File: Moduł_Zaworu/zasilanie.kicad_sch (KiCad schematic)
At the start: 25 parts, among them U1 LM2596S-ADJ, U10 LD1117S33TR_SOT223, U3 TLV172IDCK, U4 TL431D, U9 L7805

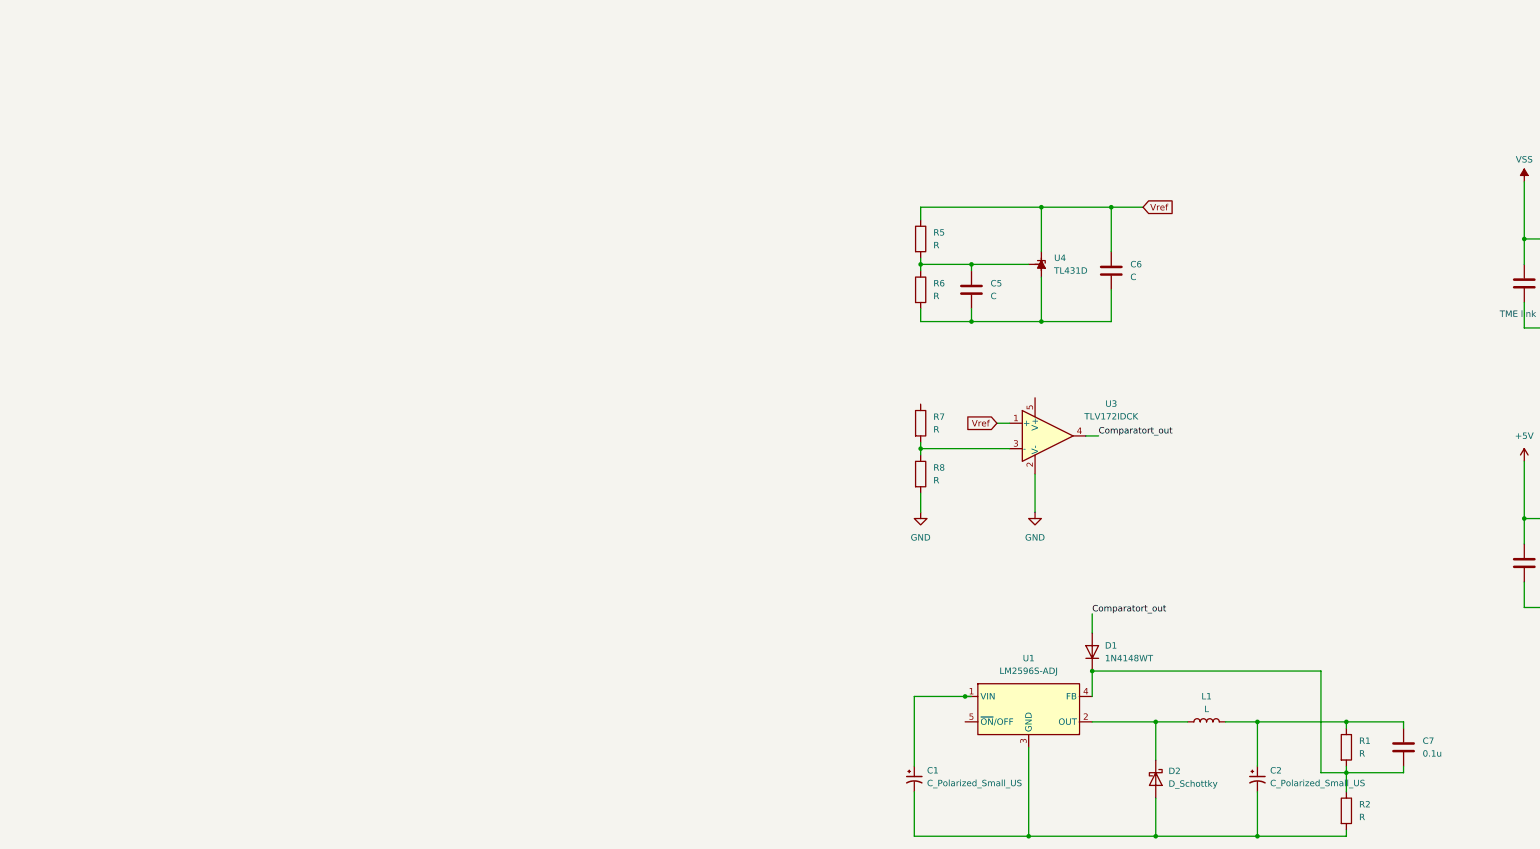
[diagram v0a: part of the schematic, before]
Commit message: Poprawki schematu modułu zaworu, usunięcie przekaźnika, przygotowanie schematu zasilania
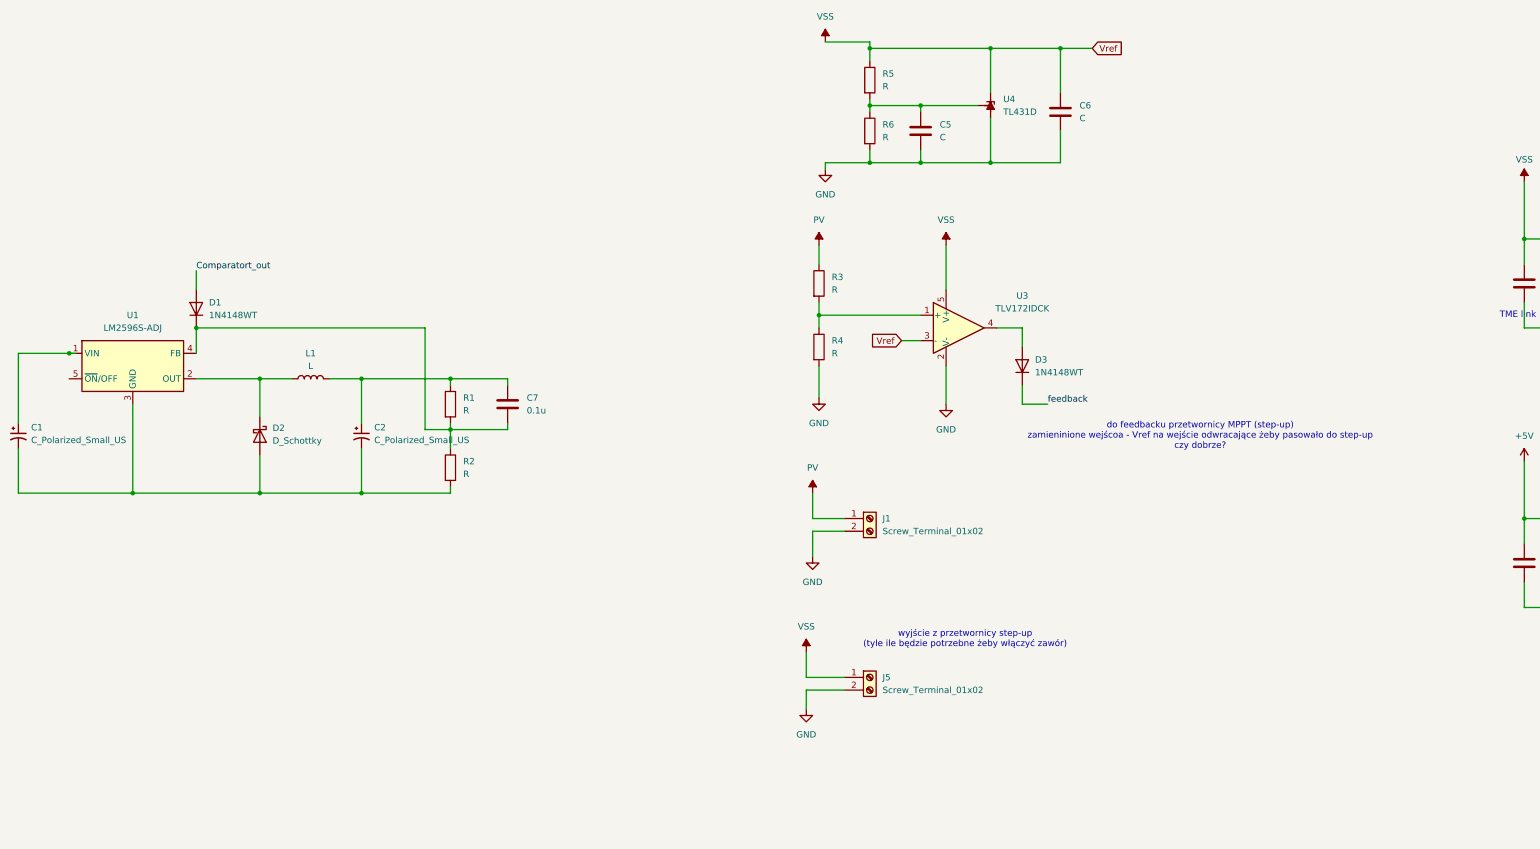
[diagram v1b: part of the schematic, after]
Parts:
- removed R7, R8: R, symbol Device:R
- added D3: 1N4148WT, Diode_SMD:D_SOD-523, symbol Diode:1N4148WT
- added J1, J5: Screw_Terminal_01x02, TerminalBlock:TerminalBlock_MaiXu_MX126-5.0-02P_1x02_P5.00mm, symbol Connector:Screw_Terminal_01x02
- added R3, R4: R, symbol Device:R
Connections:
- net Comparatort_out: no longer U3.4
- net GND: now also C5.2, C6.2, R6.2, U4.2 (A), U4.3 (A), U4.6 (A), U4.7 (A), J1.2 (Pin_2), J5.2 (Pin_2), R4.2
- net VSS: now also C6.1, R5.1, U3.3 (-), U3.5 (V+), U4.1 (K), J5.1 (Pin_1)
- removed net Vref: C6.1, R5.1, U3.1 (+), U4.1 (K)
- new net: R3.2, R4.1, U3.1 (+)
- new net: D3.2 (A), U3.4
- new net PV: J1.1 (Pin_1), R3.1
- new net feedback: D3.1 (K)
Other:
- note added: "do feedbacku przetwornicy MPPT (step-up) zamieninione wejścoa - Vref na wejście odwracające żeby pasowało do step-up czy dobrze?"
- note added: "wyjście z przetwornicy step-up (tyle ile będzie potrzebne żeby włączyć zawór)"
- moved on the sheet: C1, C2, C5, C6, C7, D1, D2, L1, R1, R2, R5, R6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

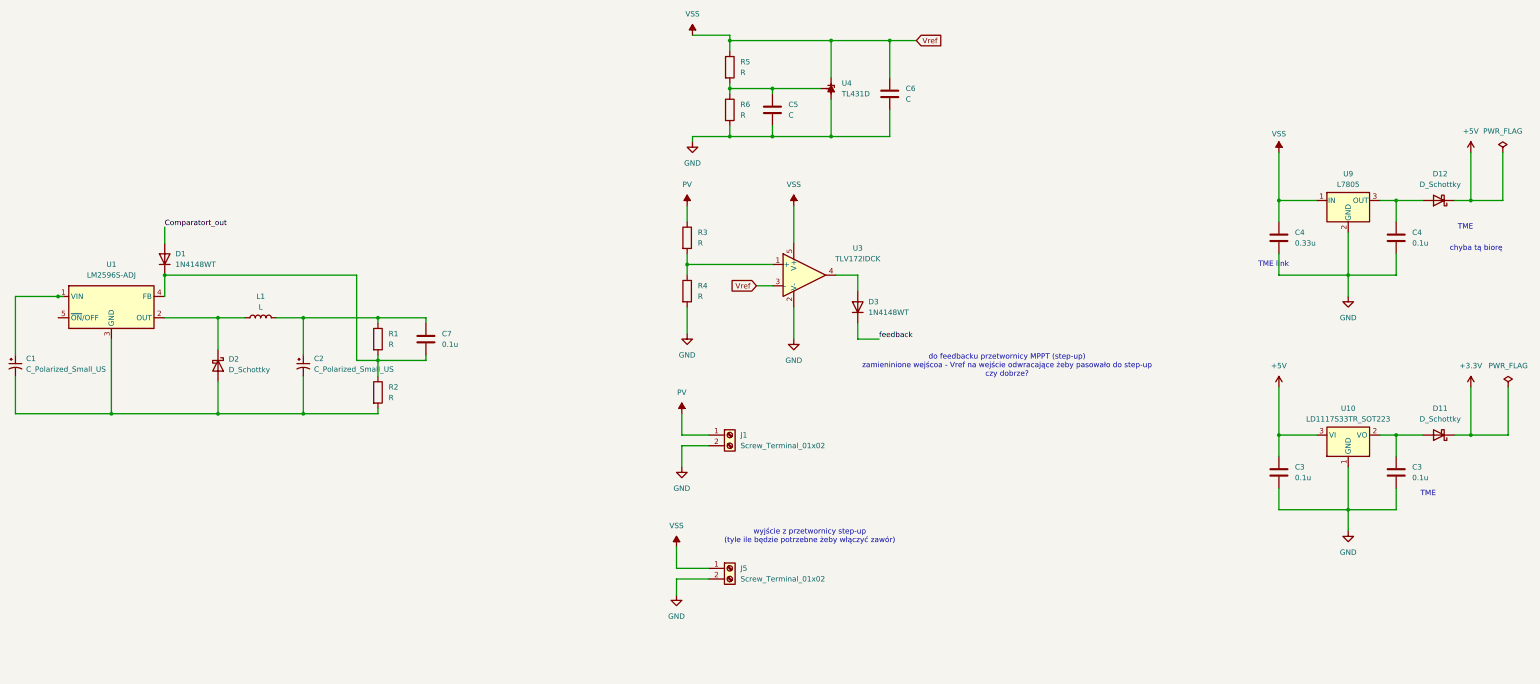
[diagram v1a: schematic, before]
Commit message: Poprawki schematu modułu zaworu, usunięcie przekaźnika, przygotowanie schematu zasilania
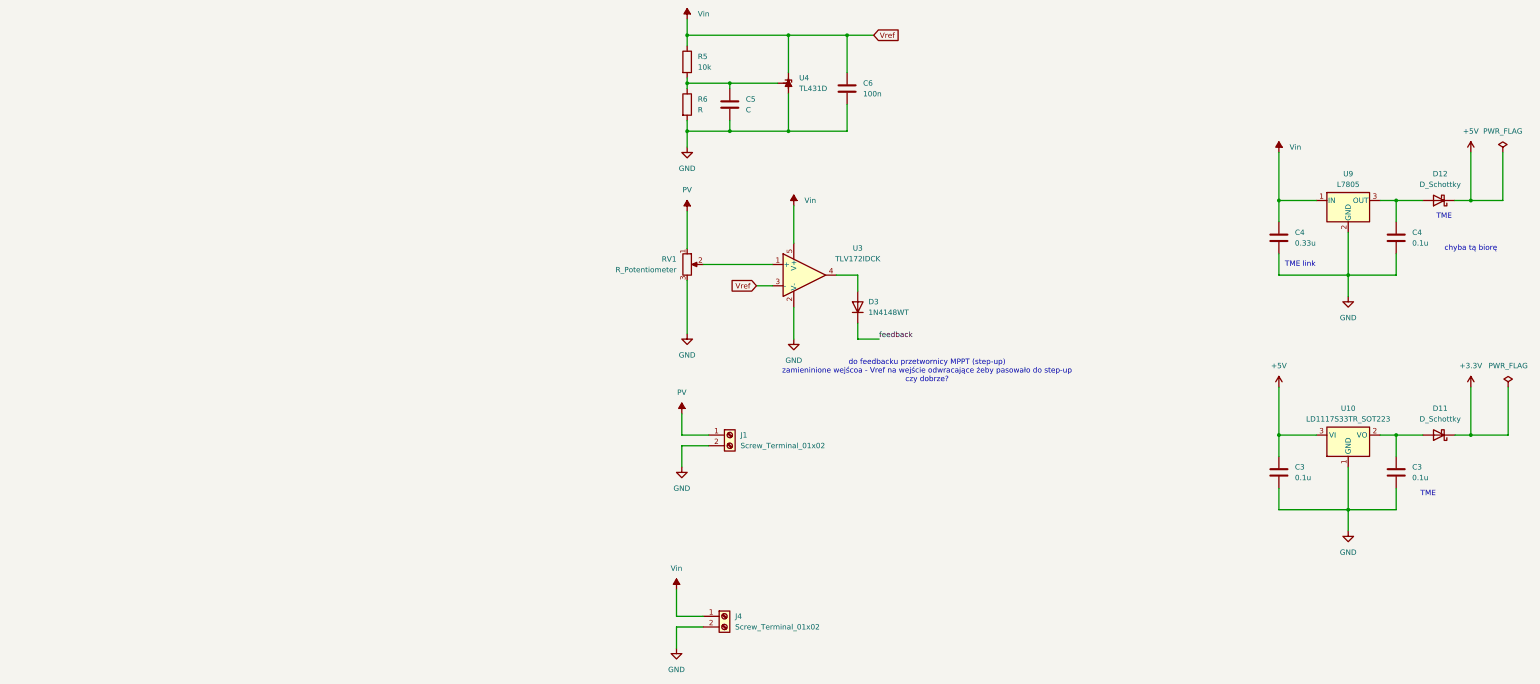
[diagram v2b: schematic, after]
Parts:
- removed C1, C2: C_Polarized_Small_US, symbol Device:C_Polarized_Small_US
- removed C7: 0.1u, Capacitor_THT:C_Disc_D3.0mm_W1.6mm_P2.50mm, symbol Device:C
- removed D1: 1N4148WT, Diode_SMD:D_SOD-523, symbol Diode:1N4148WT
- removed D2: D_Schottky, symbol Device:D_Schottky
- removed J5: Screw_Terminal_01x02, TerminalBlock:TerminalBlock_MaiXu_MX126-5.0-02P_1x02_P5.00mm, symbol Connector:Screw_Terminal_01x02
- removed L1: L, symbol Device:L
- removed R1, R2, R3, R4: R, symbol Device:R
- removed U1: LM2596S-ADJ, Package_TO_SOT_SMD:TO-263-5_TabPin3, symbol Regulator_Switching:LM2596S-ADJ
- added J4: Screw_Terminal_01x02, TerminalBlock:TerminalBlock_MaiXu_MX126-5.0-02P_1x02_P5.00mm, symbol Connector:Screw_Terminal_01x02
- added RV1: R_Potentiometer, symbol Device:R_Potentiometer
- C6: value C -> 100n
- R5: value R -> 10k
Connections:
- net GND: now also J4.2 (Pin_2), RV1.3
- net PV: now also RV1.1
- net at U3.1 (+): now also RV1.2
- net VSS renamed Vin
- net Vin: now also J4.1 (Pin_1)
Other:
- note removed: "wyjście z przetwornicy step-up (tyle ile będzie potrzebne żeby włączyć zawór)"
- moved on the sheet: C5, C6, R5, R6, U4

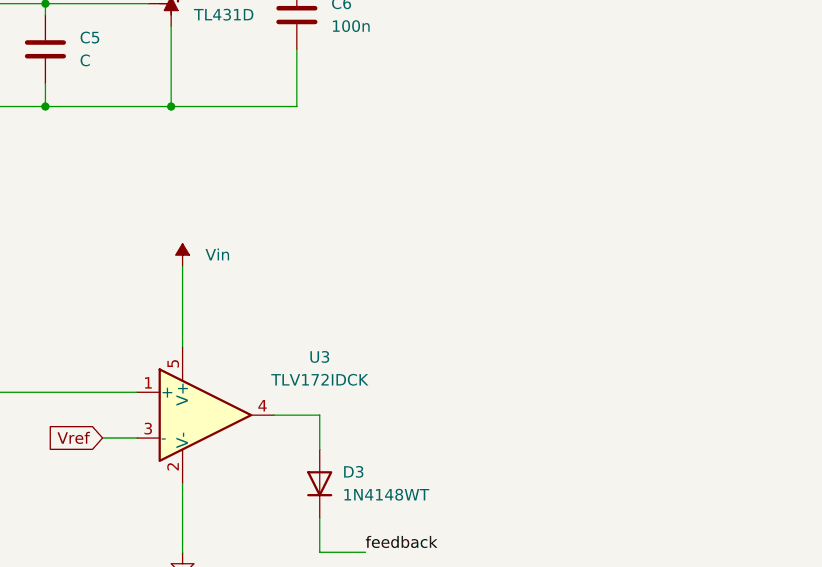
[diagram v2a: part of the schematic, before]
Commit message: Usunięcie zewnętrzego zasilania 12 i stabilizatora napięcia, korekcja zasilania wzmacniacz operacyjny moduł zasilania
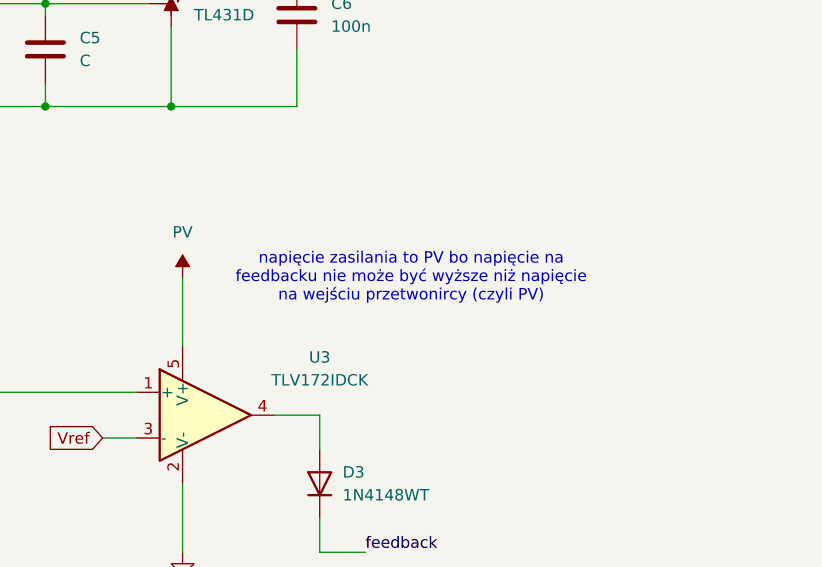
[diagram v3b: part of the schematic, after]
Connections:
- net PV: now also U3.5 (V+)
- net Vin: no longer U3.5 (V+)
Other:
- note added: "napięcie zasilania to PV bo napięcie na feedbacku nie może być wyższe niż napięcie na wejściu przetwonircy (czyli PV)"
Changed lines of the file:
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@@
+		)
+	)
+	(text "napięcie zasilania to PV bo napięcie na \nfeedbacku nie może być wyższe niż napięcie \nna wejściu przetwonircy (czyli PV)"
+		(exclude_from_sim no)
+		(at 90.17 63.5 0)
+		(effects
+			(font
+				(size 1.27 1.27)
+			)
 		)
 	)
@@
 	(wire
 		(pts
-			(xy 64.77 62.23) (xy 64.77 71.12)
+			(xy 64.77 63.5) (xy 64.77 71.12)
 		)
 		(stroke
@@
 	(symbol
 		(lib_id "power:VSS")
-		(at 64.77 62.23 0)
-		(unit 1)
-		(exclude_from_sim no)
-		(in_bom yes)
-		(on_board yes)
-		(dnp no)
-		(fields_autoplaced yes)
-		(property "Reference" "#PWR015"
-			(at 64.77 66.04 0)
-			(effects
-				(font
-					(size 1.27 1.27)
-				)
-				(hide yes)
-			)
-		)
-		(property "Value" "Vin"
-			(at 67.31 60.9599 0)
-			(effects
-				(font
-					(size 1.27 1.27)
-				)
-				(justify left)
-			)
-		)
-		(property "Footprint" ""
-			(at 64.77 62.23 0)
-			(effects
-				(font
-					(size 1.27 1.27)
-				)
-				(hide yes)
-			)
-		)
-		(property "Datasheet" ""
-			(at 64.77 62.23 0)
-			(effects
-				(font
-					(size 1.27 1.27)
-				)
-				(hide yes)
-			)
-		)
-		(property "Description" "Power symbol creates a global label with name \"VSS\""
-			(at 64.77 62.23 0)
-			(effects
-				(font
-					(size 1.27 1.27)
-				)
-				(hide yes)
-			)
-		)
-		(pin "1"
-		)
-		(instances
-			(project "Moduł_Zaworu"
-				(path "/8513fd68-b07b-4062-94bb-7b0327ec704f/94594dad-4c19-4a9b-a7b2-827222d80e0d"
-					(reference "#PWR015")
-					(unit 1)
-				)
-			)
-		)
-	)
-	(symbol
-		(lib_id "power:VSS")
 		(at 180.34 49.53 0)
 		(unit 1)
@@
 					(unit 1)
 				)
+			)
+		)
+	)
+	(symbol
+		(lib_name "PV_1")
+		(lib_id "power:PV")
+		(at 64.77 59.69 0)
+		(unit 1)
+		(exclude_from_sim no)
+		(in_bom no)
+		(on_board no)
+		(dnp no)
+		(fields_autoplaced yes)
+		(property "Reference" "#PWR012"
+			(at 65.278 58.166 0)
+			(effects
+				(font
+					(size 1.27 1.27)
+				)
+				(hide yes)
+			)
+		)
+		(property "Value" "PV"
+			(at 64.77 58.42 0)
+			(effects
+				(font
+					(size 1.27 1.27)
+				)
+			)
+		)
+		(property "Footprint" ""
+			(at 64.77 59.69 0)
+			(effects
+				(font
+					(size 1.27 1.27)
+				)
+				(hide yes)
+			)
+		)
+		(property "Datasheet" ""
+			(at 64.77 59.69 0)
+			(effects
+				(font
+					(size 1.27 1.27)
+				)
+				(hide yes)
+			)
+		)
+		(property "Description" ""
+			(at 64.77 59.69 0)
+			(effects
+				(font
+					(size 1.27 1.27)
+				)
+				(hide yes)
+			)
+		)
+		(pin "1"
+		)
+		(instances
+			(project "Moduł_Zaworu"
+				(path "/8513fd68-b07b-4062-94bb-7b0327ec704f/94594dad-4c19-4a9b-a7b2-827222d80e0d"
+					(reference "#PWR012")
+					(unit 1)
+				)
